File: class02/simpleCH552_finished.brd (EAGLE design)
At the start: 40.6 x 12 mm, 15 parts, among them U1 CH552G, X1 USBPCB

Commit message: remove fuse and test point
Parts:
- removed F1: DNP, adafruit:R1206
- removed TP1, TP2: TEST-POINT3X4, SparkFun-Connectors:PAD.03X.04
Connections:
- net +5V: no longer F1.1, F1.2
- net USB_D+: no longer TP2.P$1
- net USB_D-: no longer TP1.P$1
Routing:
- net +5V: track 71.0 -> 69.3 mm
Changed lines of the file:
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@@
 <attribute name="VALUE" x="16.621" y="7.7674" size="0.6096" layer="27" rot="R180"/>
-</element>
-<element name="F1" library="adafruit" library_urn="urn:adsk.eagle:library:420" package="R1206" value="DNP" x="15.367" y="3.429" smashed="yes">
-<attribute name="LCSC" value="C151162" x="48.387" y="-41.021" size="1.778" layer="27" display="off"/>
 </element>
 <element name="R1" library="rcl" library_urn="urn:adsk.eagle:library:334" package="R0805" package3d_urn="urn:adsk.eagle:package:23553/2" value="20K" x="31.75" y="5.9944" smashed="yes">
@@
 <attribute name="VALUE" x="11.811" y="9.0424" size="0.6096" layer="27" font="vector" ratio="20"/>
 </element>
-<element name="TP1" library="SparkFun-Connectors" library_urn="urn:adsk.eagle:library:513" package="PAD.03X.04" package3d_urn="urn:adsk.eagle:package:38287/1" value="TEST-POINT3X4" x="11.938" y="5.0292" smashed="yes"/>
-<element name="TP2" library="SparkFun-Connectors" library_urn="urn:adsk.eagle:library:513" package="PAD.03X.04" package3d_urn="urn:adsk.eagle:package:38287/1" value="TEST-POINT3X4" x="11.938" y="7.0104" smashed="yes"/>
 <element name="S1" library="SparkFun-Switches" library_urn="urn:adsk.eagle:library:535" package="TACTILE_SWITCH_SMD_6.2MM_TALL" package3d_urn="urn:adsk.eagle:package:40172/1" value="MOMENTARY-SWITCH-SPST-SMD-6.2MM-TALL" x="37.211" y="5.9944" smashed="yes" rot="R270">
 <attribute name="LCSC" value="C557616" x="37.211" y="5.9944" size="1.778" layer="27" rot="R270" display="off"/>
@@
 <wire x1="22.479" y1="6.858" x2="22.8092" y2="6.5278" width="0.254" layer="1"/>
 <wire x1="22.8092" y1="6.5278" x2="22.9616" y2="6.5278" width="0.254" layer="1"/>
-<contactref element="TP1" pad="P$1"/>
-<wire x1="11.938" y1="5.0292" x2="12.224" y2="5.0292" width="0.2032" layer="1"/>
 <wire x1="12.224" y1="5.0292" x2="12.2588" y2="4.9944" width="0.2032" layer="1"/>
 </signal>
@@
 <wire x1="29.0068" y1="9.08523125" x2="29.1084" y2="9.08523125" width="0.2032" layer="16"/>
 <wire x1="24.6634" y1="6.5024" x2="27.24623125" y2="9.08523125" width="0.2032" layer="16"/>
-<contactref element="TP2" pad="P$1"/>
-<wire x1="11.938" y1="7.0104" x2="11.9634" y2="6.985" width="0.2032" layer="1"/>
 <wire x1="11.9634" y1="6.985" x2="13.081" y2="6.985" width="0.2032" layer="1"/>
 <wire x1="29.1084" y1="9.08523125" x2="29.24408125" y2="9.08523125" width="0.2032" layer="16"/>
@@
 </signal>
 <signal name="+5V">
-<contactref element="F1" pad="2"/>
 <contactref element="C1" pad="1"/>
 <contactref element="U1" pad="15"/>
 <contactref element="R2" pad="1"/>
-<contactref element="F1" pad="1"/>
 <contactref element="X1" pad="5V"/>
 <wire x1="16.7894" y1="6.2484" x2="16.637" y2="6.2484" width="0.3048" layer="1"/>
@@
 <wire x1="16.637" y1="6.2484" x2="16.621" y2="6.2484" width="0.3048" layer="1"/>
 <wire x1="5.007" y1="2.4944" x2="10.2414" y2="2.4944" width="0.508" layer="1"/>
-<wire x1="11.176" y1="3.429" x2="13.945" y2="3.429" width="0.508" layer="1"/>
 <wire x1="10.2414" y1="2.4944" x2="11.176" y2="3.429" width="0.508" layer="1"/>
-<wire x1="16.789" y1="3.429" x2="16.789" y2="3.937" width="0.508" layer="1"/>
 <wire x1="16.789" y1="3.937" x2="16.789" y2="6.0964" width="0.508" layer="1"/>
 <wire x1="16.789" y1="6.0964" x2="16.637" y2="6.2484" width="0.508" layer="1"/>
@@
 <wire x1="19.685" y1="8.8138" x2="19.685" y2="8.001" width="0.381" layer="1"/>
 <wire x1="19.685" y1="8.001" x2="19.05" y2="7.366" width="0.381" layer="1"/>
-<wire x1="13.945" y1="3.429" x2="13.945" y2="3.912" width="0.2032" layer="1"/>
-<wire x1="13.945" y1="3.912" x2="14.859" y2="4.826" width="0.2032" layer="1"/>
-<wire x1="15.9" y1="4.826" x2="16.789" y2="3.937" width="0.2032" layer="1"/>
-<wire x1="14.859" y1="4.826" x2="15.9" y2="4.826" width="0.2032" layer="1"/>
 <via x="17.78" y="7.366" extent="1-16" drill="0.35"/>
 <wire x1="15.621" y1="11.0744" x2="15.621" y2="9.525" width="0.381" layer="16"/>
 <wire x1="15.621" y1="9.525" x2="17.78" y2="7.366" width="0.381" layer="16"/>
-<wire x1="16.789" y1="3.429" x2="17.8812" y2="4.5212" width="0.2032" layer="1"/>
 <wire x1="18.4299125" y1="4.5212" x2="18.8412" y2="4.9324875" width="0.2032" layer="1"/>
 <via x="18.8412" y="4.9324875" extent="1-16" drill="0.35"/>
 <wire x1="18.8412" y1="4.9324875" x2="19.384775" y2="4.9324875" width="0.2032" layer="16"/>
 <wire x1="19.384775" y1="4.9324875" x2="19.4404625" y2="4.8768" width="0.2032" layer="16"/>
-<wire x1="17.8812" y1="4.5212" x2="18.4299125" y2="4.5212" width="0.2032" layer="1"/>
+<wire x1="17.8812" y1="4.5212" x2="17.9832" y2="4.5212" width="0.2032" layer="1"/>
+<wire x1="17.9832" y1="4.5212" x2="18.4299125" y2="4.5212" width="0.2032" layer="1"/>
 <wire x1="19.4404625" y1="4.8768" x2="22.8759375" y2="4.8768" width="0.2032" layer="16"/>
 <wire x1="23.6633375" y1="5.6642" x2="25.025475" y2="5.6642" width="0.2032" layer="16"/>
@@
 <wire x1="39.461" y1="2.0194" x2="39.372" y2="1.9304" width="0.2032" layer="1"/>
 <wire x1="39.372" y1="1.9304" x2="38.0492" y2="1.9304" width="0.2032" layer="1"/>
+<wire x1="17.9832" y1="4.5212" x2="17.399" y2="3.937" width="0.2032" layer="1"/>
+<wire x1="17.399" y1="3.937" x2="16.789" y2="3.937" width="0.2032" layer="1"/>
+<wire x1="16.281" y1="3.429" x2="16.789" y2="3.937" width="0.508" layer="1"/>
+<wire x1="11.176" y1="3.429" x2="16.281" y2="3.429" width="0.508" layer="1"/>
 </signal>
 <signal name="P1.4">

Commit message: move parts
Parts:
- moved C1 2.07 mm to (14.6, 4.45)
- moved C2 1.55 mm to (14.6, 7.62)
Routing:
- net 3.3V: track 1.80 -> 3.46 mm
- net USB_D+: track 32.6 -> 31.5 mm
- net GND: track 64.0 -> 64.9 mm

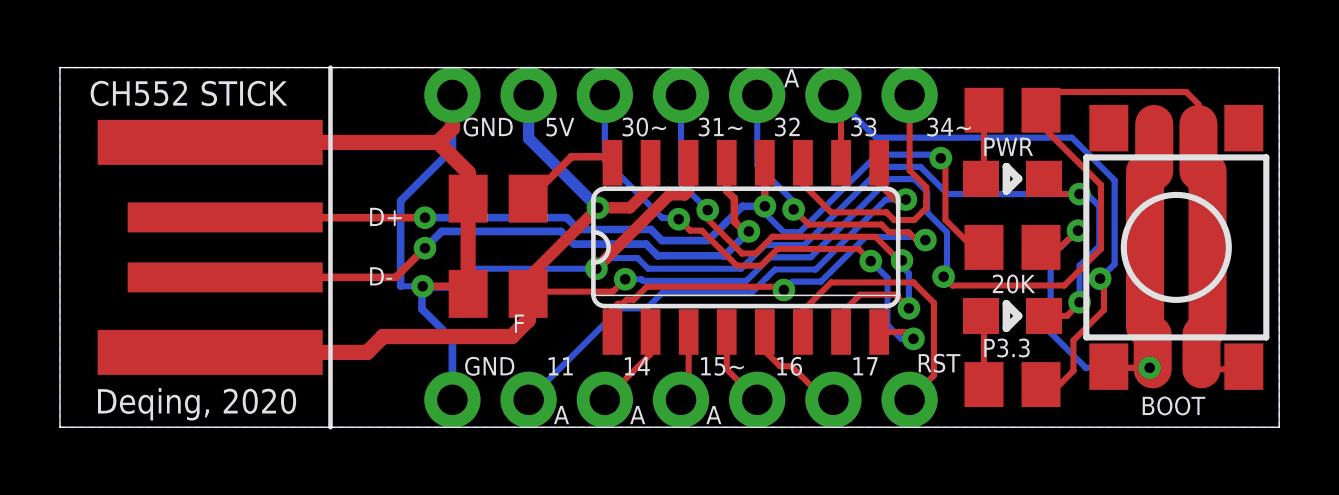
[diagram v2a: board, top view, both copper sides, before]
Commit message: update to USB shell model
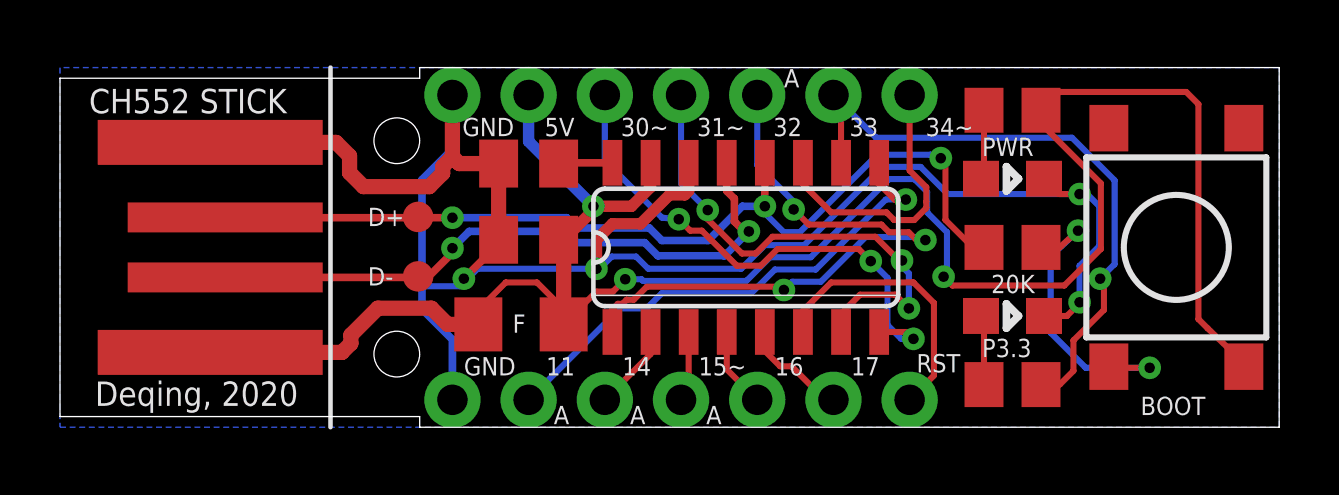
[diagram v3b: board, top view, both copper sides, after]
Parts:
- added F1: (no value), adafruit:R1206
- added TP1, TP2: TEST-POINT3X4, SparkFun-Connectors:PAD.03X.04
- moved C1 2.07 mm to (15.6, 6.25)
- moved C2 1.55 mm to (15.6, 8.79)
- renumbered U1 to U2
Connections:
- net +5V: now also F1.1, F1.2
- net USB_D+: now also TP2.P$1
- net USB_D-: now also TP1.P$1
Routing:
- net N$1: track 19.1 -> 10.4 mm
- net 3.3V: track 3.46 -> 1.80 mm
- net USB_D+: track 31.5 -> 32.6 mm
- net +5V: track 69.3 -> 70.2 mm
- net GND: track 64.9 -> 65.6 mm
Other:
- outline, holes or cut-outs redrawn
- board text added: "Deqing Sun, 2020 Try Ch55xduino with this board"
- board text added: "Deqing Sun, 2022 Prototyping Electronic Devices"
- board text removed: "Deqing Sun, 2020 Prototyping Electronic Devices"
